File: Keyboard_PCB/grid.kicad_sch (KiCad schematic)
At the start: 31 parts, among them SW10 7, SW11 8, SW12 9, SW13 10, SW14 11, SW15 EC11E15244G1, SW3 0, SW4 1, SW5 2, SW6 3, SW7 4, SW8 5, SW9 6

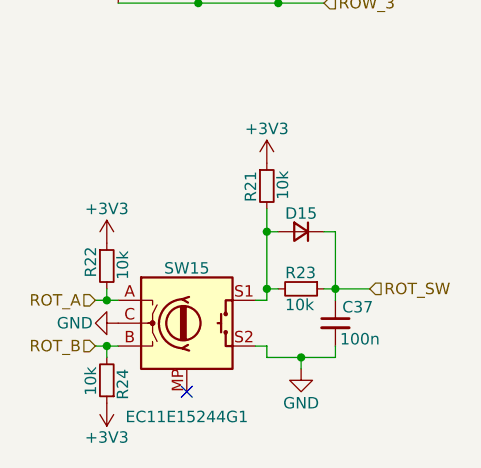
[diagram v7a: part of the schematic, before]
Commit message: Added active battery sensing circuit
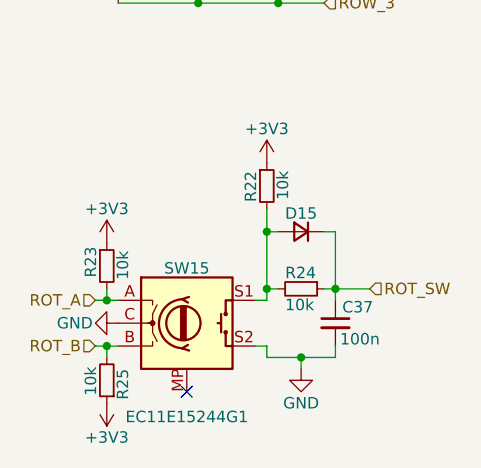
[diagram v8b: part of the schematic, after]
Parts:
- renumbered R21 to R22, R22 to R23, R23 to R24, R24 to R25
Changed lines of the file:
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@@
 		(on_board yes)
 		(dnp no)
-		(property "Reference" "R22"
+		(property "Reference" "R23"
 			(at 62.992 148.59 90)
 			(effects
@@
 			(project "Keyboard_PCB"
 				(path "/dd51e792-c76c-4d43-96de-494177f3b593/2efb7614-f68d-465d-9514-3e61f2b99fcc"
-					(reference "R22")
+					(reference "R23")
 					(unit 1)
 				)
@@
 		(on_board yes)
 		(dnp no)
-		(property "Reference" "R21"
+		(property "Reference" "R22"
 			(at 80.772 140.208 90)
 			(effects
@@
 			(project "Keyboard_PCB"
 				(path "/dd51e792-c76c-4d43-96de-494177f3b593/2efb7614-f68d-465d-9514-3e61f2b99fcc"
-					(reference "R21")
+					(reference "R22")
 					(unit 1)
 				)
@@
 		(on_board yes)
 		(dnp no)
-		(property "Reference" "R23"
+		(property "Reference" "R24"
 			(at 84.582 148.082 90)
 			(effects
@@
 			(project "Keyboard_PCB"
 				(path "/dd51e792-c76c-4d43-96de-494177f3b593/2efb7614-f68d-465d-9514-3e61f2b99fcc"
-					(reference "R23")
+					(reference "R24")
 					(unit 1)
 				)
@@
 		(on_board yes)
 		(dnp no)
-		(property "Reference" "R24"
+		(property "Reference" "R25"
 			(at 66.548 158.75 90)
 			(effects
@@
 			(project "Keyboard_PCB"
 				(path "/dd51e792-c76c-4d43-96de-494177f3b593/2efb7614-f68d-465d-9514-3e61f2b99fcc"
-					(reference "R24")
-					(unit 1)
-				)
+					(reference "R25")
+					(unit 1)
+				)
